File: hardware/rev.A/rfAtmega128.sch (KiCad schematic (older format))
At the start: 58 parts, among them J3 PWR_ON/OFF, J4 J2PIN, J5 J2PIN, U1 LED_RED, U10 LED_GREEN, U11 LED_GREEN, U12 LED_GREEN, U13 BAT54S, U14 BAT54S, U2 DIODE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

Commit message: Added BOM of the board and fixed some resistor values in the schematic.
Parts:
- R15, R16: value RES_0603 -> 510
- R2: value RES_0603 -> 100K
- R8, R9: value RES_0603 -> 2.7K
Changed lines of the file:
@@
-EESchema Schematic File Version 2  date Tue 12 Jun 2012 11:07:18 AM EEST
+EESchema Schematic File Version 2  date Mon 16 Jul 2012 04:51:59 PM EEST
 LIBS:power
 LIBS:conn
@@
 Sheet 1 1
 Title ""
-Date "5 jun 2012"
+Date "16 jul 2012"
 Rev ""
 Comp ""
@@
 P 5600 4300
 F 0 "R8" H 5600 4300 39  0000 C CNN
-F 1 "RES_0603" H 5600 4400 39  0001 C CNN
+F 1 "2.7K" H 5600 4400 39  0001 C CNN
 F 2 "r_0603" H 5600 4300 60  0001 C CNN
 	1    5600 4300
@@
 P 5800 4300
 F 0 "R9" H 5800 4300 39  0000 C CNN
-F 1 "RES_0603" H 5800 4400 39  0001 C CNN
+F 1 "2.7K" H 5800 4400 39  0001 C CNN
 F 2 "r_0603" H 5800 4300 60  0001 C CNN
 	1    5800 4300
@@
 P 8200 3100
 F 0 "R15" H 8200 3100 39  0000 C CNN
-F 1 "RES_0603" H 8200 3200 39  0001 C CNN
+F 1 "510" H 8200 3200 39  0001 C CNN
 F 2 "r_0603" H 8200 3100 60  0001 C CNN
 	1    8200 3100
@@
 P 8200 3050
 F 0 "R16" H 8200 3050 39  0000 C CNN
-F 1 "RES_0603" H 8200 3150 39  0001 C CNN
+F 1 "510" H 8200 3150 39  0001 C CNN
 F 2 "r_0603" H 8200 3050 60  0001 C CNN
 	1    8200 3050
@@
 P 1950 950
 F 0 "R2" H 1950 950 39  0000 C CNN
-F 1 "RES_0603" H 1950 1050 39  0001 C CNN
+F 1 "100K" H 1950 1050 39  0001 C CNN
 F 2 "r_0603" H 1950 950 39  0001 C CNN
 	1    1950 950

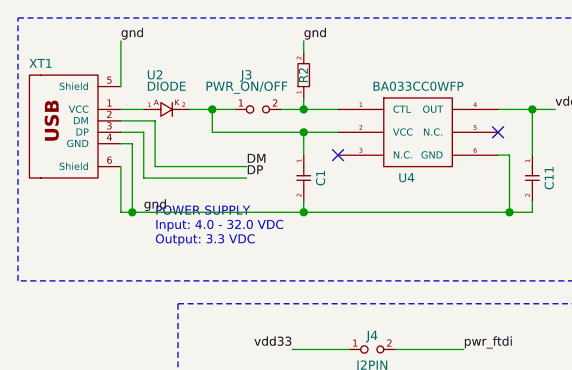
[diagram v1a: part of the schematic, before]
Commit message: Changed D1 to 1N4007 in the schematic.
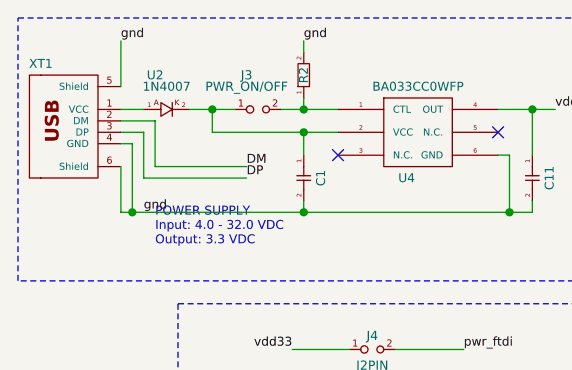
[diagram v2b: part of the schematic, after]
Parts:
- U2: value DIODE -> 1N4007
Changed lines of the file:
@@
-EESchema Schematic File Version 2  date Mon 16 Jul 2012 04:51:59 PM EEST
+EESchema Schematic File Version 2  date Wed 18 Jul 2012 10:25:55 AM EEST
 LIBS:power
 LIBS:conn
@@
 Sheet 1 1
 Title ""
-Date "16 jul 2012"
+Date "18 jul 2012"
 Rev ""
 Comp ""
@@
 P 1350 1100
 F 0 "U2" H 1300 1250 39  0000 C CNN
-F 1 "DIODE" H 1350 1200 39  0000 C CNN
+F 1 "1N4007" H 1350 1200 39  0000 C CNN
 F 2 "melf" H 1350 1100 60  0001 C CNN
 F 3 "http://store.comet.bg/bg/Catalogue/Product/27933/" H 1350 1100 39  0001 C CNN

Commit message: Pins swapped of the RX and TX protective diodes marked on schematic. Resistor values of R6 and R7 changed to 0 in BOM and netlist.
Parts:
- R6, R7: value 510 -> 0
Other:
- note added: "PINS SWAPED\nSHORT THE PWR"
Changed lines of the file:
@@
-EESchema Schematic File Version 2  date Wed 18 Jul 2012 10:25:55 AM EEST
+EESchema Schematic File Version 2  date Fri 20 Jul 2012 05:45:53 PM EEST
 LIBS:power
 LIBS:conn
@@
 Sheet 1 1
 Title ""
-Date "18 jul 2012"
+Date "20 jul 2012"
 Rev ""
 Comp ""
@@
 Comment4 ""
 $EndDescr
+Wire Notes Line
+	7900 3600 7900 3500
+Wire Notes Line
+	7900 3500 7700 3500
 Wire Wire Line
 	1150 1350 1150 1550
@@
 Wire Notes Line
 	7300 5200 7300 2650
+Wire Notes Line
+	7700 3200 7350 3200
+Wire Notes Line
+	7700 3200 7700 3550
+Wire Notes Line
+	7700 3550 7350 3550
+Wire Notes Line
+	7350 3550 7350 3200
+Text Notes 7776 3672 0    39   ~ 0
+PINS SWAPED\nSHORT THE PWR
 $Comp
 L USB_B XT1
@@
 P 4350 1350
 F 0 "R7" H 4350 1350 39  0000 C CNN
-F 1 "510" H 4350 1450 39  0001 C CNN
+F 1 "0" H 4350 1450 39  0001 C CNN
 F 2 "r_0603" H 4350 1350 60  0001 C CNN
 	1    4350 1350
@@
 P 4350 1300
 F 0 "R6" H 4350 1300 39  0000 C CNN
-F 1 "510" H 4350 1400 39  0001 C CNN
+F 1 "0" H 4350 1400 39  0001 C CNN
 F 2 "r_0603" H 4350 1300 60  0001 C CNN
 	1    4350 1300

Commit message: Added some documentation files and updated schematic.
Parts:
- C2, C3: value 100n -> 20n
- R5: value 100K -> 30K
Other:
- note added: "ADDED MCP809 TO RESET PIN"
- note added: "DON'T MOUNT ON BOARD"
- note added: "R12 replaced with CAP 0603 = 100nF"
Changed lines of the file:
@@
-EESchema Schematic File Version 2  date Fri 20 Jul 2012 05:45:53 PM EEST
+EESchema Schematic File Version 2  date Fri 26 Oct 2012 01:14:30 PM EEST
 LIBS:power
 LIBS:conn
@@
 Sheet 1 1
 Title ""
-Date "20 jul 2012"
+Date "26 oct 2012"
 Rev ""
 Comp ""
@@
 $EndDescr
 Wire Notes Line
+	7550 3550 7550 3800
+Wire Notes Line
+	7550 3800 7750 3800
+Wire Notes Line
 	7900 3600 7900 3500
 Wire Notes Line
@@
 Wire Notes Line
 	7350 3550 7350 3200
+Wire Notes Line
+	3750 3000 3500 3000
+Wire Notes Line
+	3500 3000 3500 3300
+Text Notes 7750 3850 0    60   ~ 0
+DON'T MOUNT ON BOARD
+Text Notes 5350 850  0    60   ~ 0
+R12 replaced with CAP 0603 = 100nF
+Text Notes 3750 3050 0    60   ~ 0
+ADDED MCP809 TO RESET PIN
 Text Notes 7776 3672 0    39   ~ 0
 PINS SWAPED\nSHORT THE PWR
@@
 P 1950 3550
 F 0 "C3" H 1950 3500 39  0000 C CNN
-F 1 "100n" H 1950 3600 39  0000 C CNN
+F 1 "20n" H 1950 3600 39  0000 C CNN
 F 2 "c_0603" H 1950 3550 60  0001 C CNN
 	1    1950 3550
@@
 P 1950 3100
 F 0 "C2" H 1950 3050 39  0000 C CNN
-F 1 "100n" H 1950 3150 39  0000 C CNN
+F 1 "20n" H 1950 3150 39  0000 C CNN
 F 2 "c_0603" H 1950 3100 60  0001 C CNN
 	1    1950 3100
@@
 P 3450 3150
 F 0 "R5" H 3450 3150 39  0000 C CNN
-F 1 "100K" H 3450 3250 39  0001 C CNN
+F 1 "30K" H 3450 3250 39  0001 C CNN
 F 2 "r_0603" H 3450 3150 60  0001 C CNN
 	1    3450 3150

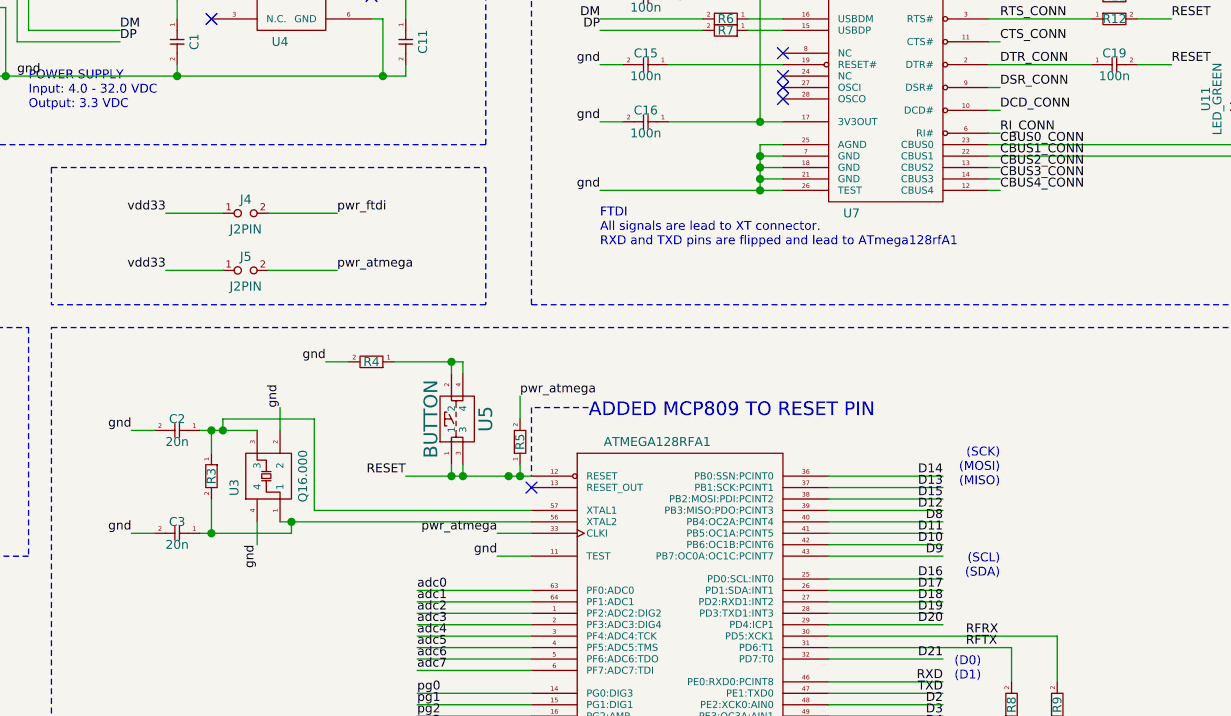
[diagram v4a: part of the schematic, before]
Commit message: Added Zigduino Radio Examples, CW and Spectrum analyzer
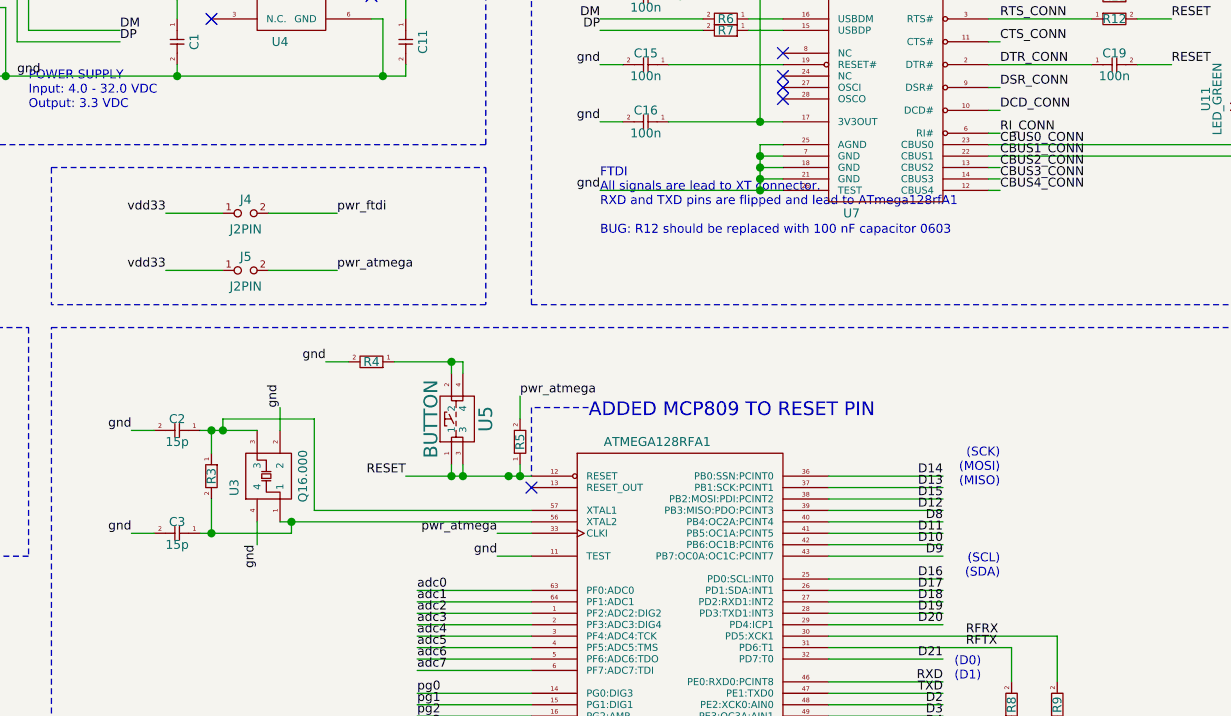
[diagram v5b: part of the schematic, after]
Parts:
- C2, C3: value 20n -> 15p
- R3: value 1M -> do not mount
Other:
- note added: "FTDI\nAll signals are lead to XT connector.\nRXD and TXD pins are flipped and lead to ATmega128rfA1\n\nBUG: R12 should be replaced with 100 nF capacitor 0603"
- note removed: "FTDI\nAll signals are lead to XT connector.\nRXD and TXD pins are flipped and lead to ATmega128rfA1"
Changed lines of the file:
@@
-EESchema Schematic File Version 2  date Fri 26 Oct 2012 01:14:30 PM EEST
+EESchema Schematic File Version 2  date Thu 10 Jan 2013 12:49:49 PM EET
 LIBS:power
 LIBS:conn
 LIBS:rfAtmega128schlib
 LIBS:rfAtmega128-cache
-EELAYER 25  0
+EELAYER 27 0
 EELAYER END
-$Descr A4 11700 8267
+$Descr A4 11693 8268
 encoding utf-8
 Sheet 1 1
 Title ""
-Date "26 oct 2012"
+Date "10 jan 2013"
 Rev ""
 Comp ""
@@
 P 2100 3300
 F 0 "R3" H 2100 3300 39  0000 C CNN
-F 1 "1M" H 2100 3400 39  0001 C CNN
+F 1 "do not mount" H 2100 3400 39  0001 C CNN
 F 2 "r_0603" H 2100 3300 60  0001 C CNN
 	1    2100 3300
@@
 P 1950 3550
 F 0 "C3" H 1950 3500 39  0000 C CNN
-F 1 "20n" H 1950 3600 39  0000 C CNN
+F 1 "15p" H 1950 3600 39  0000 C CNN
 F 2 "c_0603" H 1950 3550 60  0001 C CNN
 	1    1950 3550
@@
 P 1950 3100
 F 0 "C2" H 1950 3050 39  0000 C CNN
-F 1 "20n" H 1950 3150 39  0000 C CNN
+F 1 "15p" H 1950 3150 39  0000 C CNN
 F 2 "c_0603" H 1950 3100 60  0001 C CNN
 	1    1950 3100
@@
 	1    0    0    -1
 $EndComp
-Text Notes 3800 2300 0    39   ~ 0
-FTDI\nAll signals are lead to XT connector.\nRXD and TXD pins are flipped and lead to ATmega128rfA1
+Text Notes 3800 2250 0    39   ~ 0
+FTDI\nAll signals are lead to XT connector.\nRXD and TXD pins are flipped and lead to ATmega128rfA1\n\nBUG: R12 should be replaced with 100 nF capacitor 0603
 Text Label 6750 1100 0    39   ~ 0
 pwr_ftdi
